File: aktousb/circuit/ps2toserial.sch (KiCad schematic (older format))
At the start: 19 parts, among them IC1 ATMEGA8-P, X1 16MHz

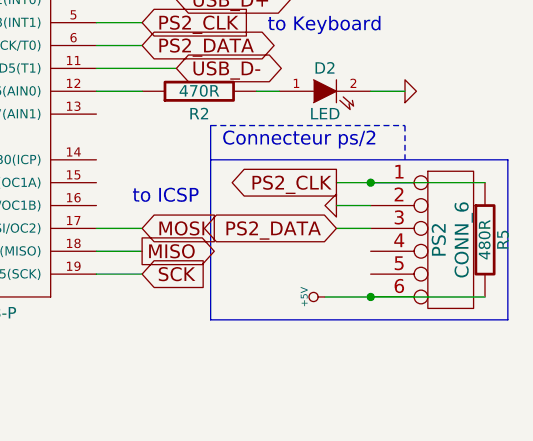
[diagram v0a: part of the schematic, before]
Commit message: Correction d'un bug de routage du PCB : le +5V était sur la mauvaise patte du connecteur clavier.
git-svn-id: svn://pulkomandy.tk/avrstuff@16 c6672c3c-f6b6-47f9-9001-1fd6b12fecbe
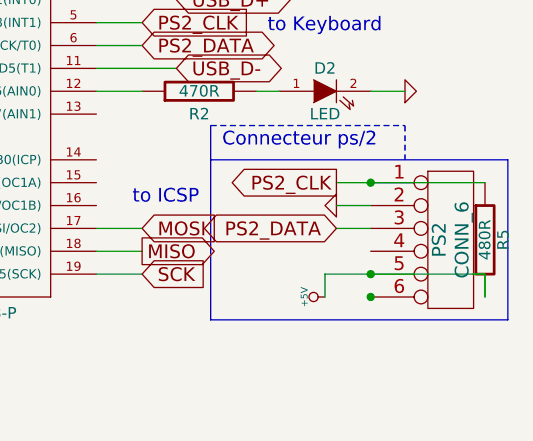
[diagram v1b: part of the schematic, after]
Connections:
- net +5V: now also PS2.5; no longer PS2.6
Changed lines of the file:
@@
-EESchema Schematic File Version 2  date 30/07/2010 20:15:21
+EESchema Schematic File Version 2  date 30/08/2010 19:46:30
 LIBS:power
 LIBS:device
@@
 Sheet 1 1
 Title "PS/2 to serial converter"
-Date "30 jul 2010"
+Date "30 aug 2010"
 Rev "2010.06.22"
 Comp "PulkoTronics"
@@
 Comment4 ""
 $EndDescr
+Connection ~ 4550 4000
+Wire Wire Line
+	5050 4100 5050 4000
+Wire Wire Line
+	5050 4000 4350 4000
 Wire Wire Line
 	4500 2350 4250 2350
@@
 	1900 650  1900 1150
 Connection ~ 4550 3600
-Wire Wire Line
-	4350 4100 5050 4100
 Connection ~ 4550 4100
 Wire Wire Line
@@
 Wire Wire Line
 	4350 2600 4500 2600
+Wire Wire Line
+	4350 4000 4350 4100
 $Comp
 L JUMPER JP1
